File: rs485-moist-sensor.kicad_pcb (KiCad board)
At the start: 2 copper layers, 20 x 140 mm, 26 parts, among them IC1 ATTINY441-MU, P1 CONN_02X03, P2 CONN_01X04, U1 SP3481EN, X1 16MHz

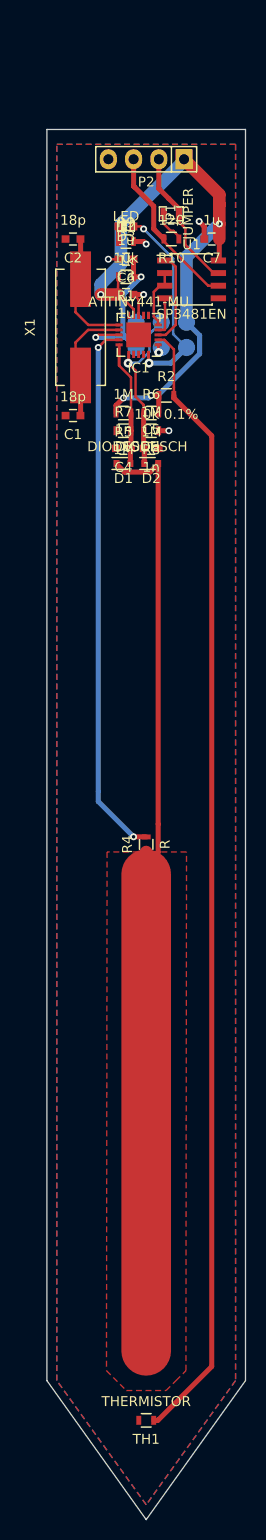
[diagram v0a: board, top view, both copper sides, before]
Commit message: Move trace so that it does not touch a square MOSI pad
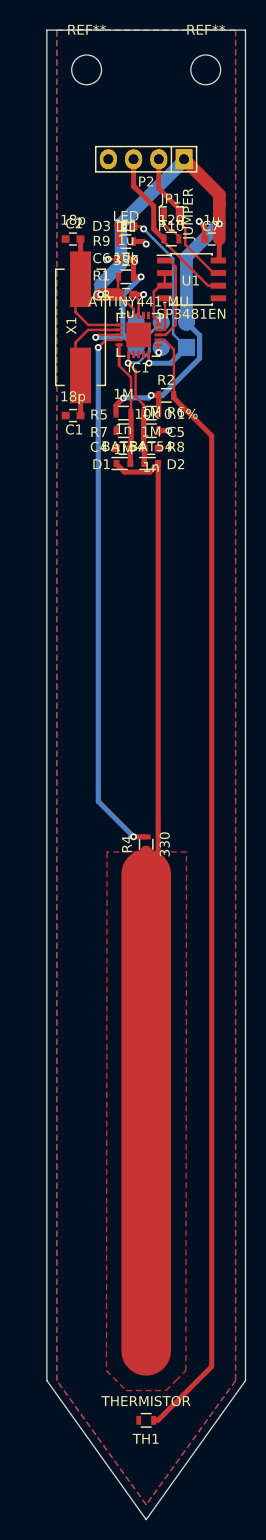
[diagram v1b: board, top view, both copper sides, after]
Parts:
- added REF**: MountingHole_3mm, Mounting_Holes:MountingHole_3mm, F.Cu at (89.0, 17.0)
- added REF**: MountingHole_3mm, Mounting_Holes:MountingHole_3mm, F.Cu at (101.0, 17.0)
- D1, D2: value DIODESCH -> BAT54
- R4: value R -> 330
- R9: value 1k -> 330
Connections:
- U1 pad 1: Net-(IC1-Pad3) -> Net-(IC1-Pad4)
- U1 pad 2: Net-(IC1-Pad5) -> Net-(IC1-Pad3)
- U1 pad 4: Net-(IC1-Pad4) -> Net-(IC1-Pad5)
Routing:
- net Net-(IC1-Pad4): track 3.84 -> 4.66 mm
- net Net-(IC1-Pad5): track 6.14 -> 5.42 mm
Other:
- board size 20 x 140 mm -> 20 x 150 mm

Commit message: Fiddle around with RS485 transceiver lib symbol -- pins were dangerously swapped!
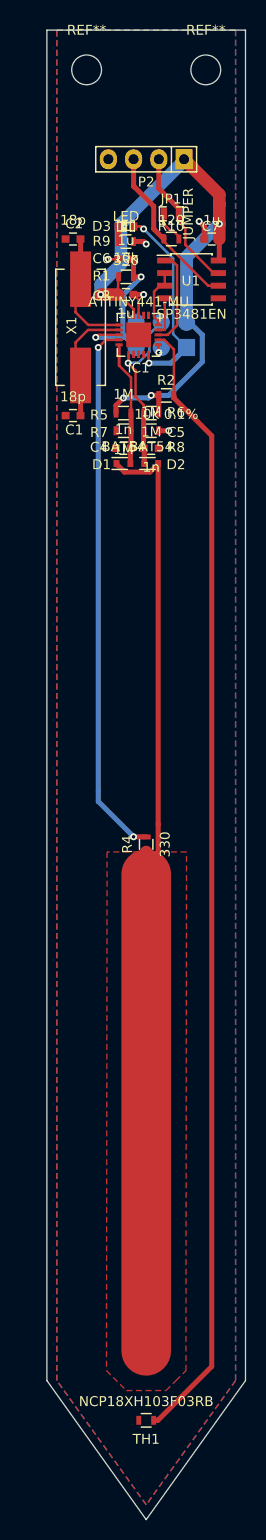
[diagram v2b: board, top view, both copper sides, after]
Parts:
- TH1: value THERMISTOR -> NCP18XH103F03RB
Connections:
- U1 pad 1: Net-(IC1-Pad4) -> Net-(IC1-Pad3)
- U1 pad 2: Net-(IC1-Pad3) -> Net-(IC1-Pad5)
- U1 pad 4: Net-(IC1-Pad5) -> Net-(IC1-Pad4)
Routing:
- net Net-(IC1-Pad5): track 5.42 -> 6.59 mm
- net VCC: track 64.3 -> 65.1 mm

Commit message: Add a local voltage regulator, add antistatic protection, specify transceiver, change attiny441 package to soic-14, route everything
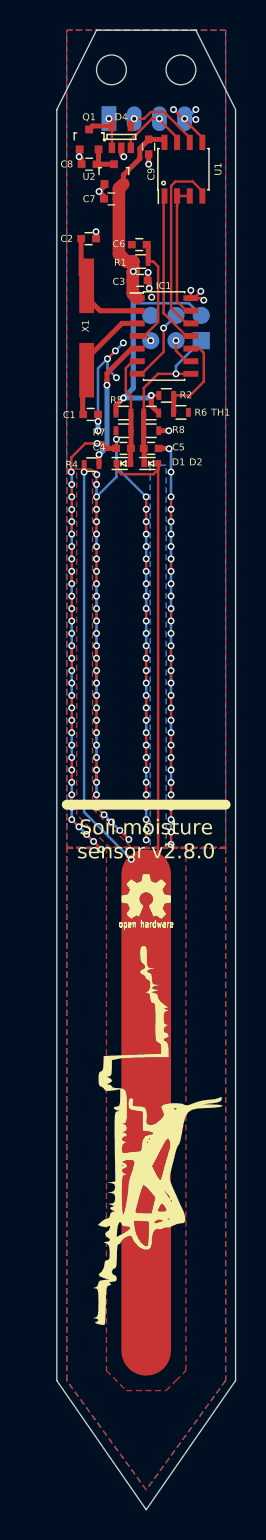
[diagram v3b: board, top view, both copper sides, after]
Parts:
- removed D3: LED, LEDs:LED-0603
- removed JP1: JUMPER, SMD_Packages:SMD-0603_r
- removed R10: 120, Resistors_SMD:R_0603
- removed R9: 330, Resistors_SMD:R_0603
- added C8: 1u, Capacitors_SMD:C_0603, F.Cu at (89.2, 26.5)
- added C9: 1u, Capacitors_SMD:C_0603, F.Cu at (95.2, 24.8)
- added D4: NUP4004M5T1G, Housings_SOT-23_SOT-143_TSOT-6:SOT-23-5, F.Cu at (92.5, 23.8)
- added G***: LOGO, w_logo:Logo_silk_OSHW_6x6mm, F.Cu at (95.0, 100.2)
- added G***: LOGO, chirp_logo:ziogas, B.Cu at (96.2, 124.2)
- added Q1: Q_PMOS_GSD, Housings_SOT-23_SOT-143_TSOT-6:SOT-23, F.Cu at (89.2, 24.0)
- added U2: MCP1702, Housings_SOT-23_SOT-143_TSOT-6:SOT-23, F.Cu at (91.8, 27.5)
- IC1: value ATTINY441-MU -> ATTINY441-SSU; footprint Housings_DFN_QFN:QFN-20-1EP_4x4mm_Pitch0.5mm -> Housings_SOIC:SOIC-14_3.9x8.7mm_Pitch1.27mm
- P1: value CONN_02X03 -> AVR ISP6
- P2: footprint Pin_Headers:Pin_Header_Straight_1x04 -> Pin_Headers:Pin_Header_Straight_1x04_Pitch2.54mm; moved to B.Cu
- U1: value SP3481EN -> SN65HVD72
- moved TH1 101.6 mm to (98.5, 51.5), turned to 0 degrees
- moved R4 38.6 mm to (89.5, 56.8), turned to 0 degrees
- moved U1 11.1 mm to (98.8, 27.0), turned to 90 degrees
- moved C7 10.9 mm to (91.5, 30.0)
- moved P2 5.54 mm to (91.2, 21.9), turned to 270 degrees
- moved IC1 2.57 mm to (96.8, 43.8), turned to 0 degrees
- moved REF** 2.50 mm to (91.5, 17.0)
- moved REF** 2.50 mm to (98.5, 17.0)
- moved R1 2.14 mm to (94.5, 36.3)
- moved C3 2.02 mm to (94.4, 38.2)
- moved C6 1.98 mm to (94.3, 34.6)
- moved C1 1.77 mm to (89.4, 51.7), turned to 0 degrees
- moved P1 1.63 mm to (98.0, 43.0)
- moved C2 1.57 mm to (89.2, 34.0), turned to 0 degrees
- moved X1 0.61 mm to (89.0, 43.0)
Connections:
- C3 pad 1: VCC -> +3V3
- C5 pad 1: /SENSE_HIGH/MOSI -> /SENSE_HIGH/MISO
- C7 pad 1: VCC -> +3V3
- D2 pad 2: /SENSE_HIGH/MOSI -> /SENSE_HIGH/MISO
- IC1 pad 1: /SCK -> +3V3
- IC1 pad 10: (no net) -> /THERMISTOR
- IC1 pad 11: Net-(C2-Pad1) -> Net-(IC1-Pad11)
- IC1 pad 12: Net-(C1-Pad1) -> Net-(IC1-Pad12)
- IC1 pad 13: /RESET -> Net-(IC1-Pad13)
- IC1 pad 14: /EXCITATION -> GND
- IC1 pad 2: /THERMISTOR -> Net-(C2-Pad1)
- IC1 pad 3: Net-(IC1-Pad3) -> Net-(C1-Pad1)
- IC1 pad 4: Net-(IC1-Pad4) -> /RESET
- IC1 pad 5: Net-(IC1-Pad5) -> /EXCITATION
- IC1 pad 6: (no net) -> /SENSE_LOW
- IC1 pad 7: (no net) -> /MOSI
- IC1 pad 8: GND -> /SENSE_HIGH/MISO
- IC1 pad 9: VCC -> /SCK
- P1 pad 1: /MISO -> /SENSE_HIGH/MISO
- P1 pad 2: VCC -> +3V3
- P1 pad 4: /SENSE_HIGH/MOSI -> /MOSI
- P2 pad 2: /RS485B -> /RS485A
- P2 pad 3: /RS485A -> /RS485B
- R1 pad 2: VCC -> +3V3
- R2 pad 1: VCC -> +3V3
- R5 pad 2: VCC -> +3V3
- R6 pad 1: /SENSE_HIGH/MOSI -> /SENSE_HIGH/MISO
- R6 pad 2: VCC -> +3V3
- R8 pad 2: /SENSE_HIGH/MOSI -> /SENSE_HIGH/MISO
- U1 pad 1: Net-(IC1-Pad3) -> Net-(IC1-Pad11)
- U1 pad 2: Net-(IC1-Pad5) -> Net-(IC1-Pad13)
- U1 pad 3: Net-(IC1-Pad5) -> Net-(IC1-Pad13)
- U1 pad 4: Net-(IC1-Pad4) -> Net-(IC1-Pad12)
- U1 pad 8: VCC -> +3V3
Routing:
- net GND: track 8.72 -> 219.9 mm, vias 5 -> 148
- net /THERMISTOR: track 114.1 -> 9.70 mm
- net VCC: track 65.1 -> 5.75 mm, vias 4 -> 1
- net +3V3: track 0.00 -> 48.5 mm, vias 0 -> 3
- net /SENSOR_TRACK: track 98.0 -> 140.8 mm, vias 0 -> 2
- net /EXCITATION: track 54.4 -> 13.6 mm
- net /MISO: track 20.2 -> 0.00 mm, vias 2 -> 0
- net Net-(IC1-Pad12): track 0.00 -> 19.1 mm
- net /SENSE_HIGH/MISO: track 0.00 -> 17.7 mm, vias 0 -> 1
- net /SENSE_HIGH/MOSI: track 17.7 -> 0.00 mm, vias 1 -> 0
- net Net-(IC1-Pad11): track 0.00 -> 15.5 mm
- net Net-(IC1-Pad13): track 0.00 -> 13.7 mm
- net Net-(IC1-Pad3): track 9.79 -> 0.00 mm
- net /RS485A: track 17.2 -> 8.28 mm, vias 0 -> 1
- net /MOSI: track 0.00 -> 7.76 mm, vias 0 -> 1
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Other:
- board size 20 x 150 mm -> 18 x 149 mm
- net class excitation added: clearance 0.6, trace_width 0.254, via_dia 0.7, via_drill 0.4
- board text added: "Catnip Electronics mic@wemakethings.net https://github.com/Miceuz/rs485-moist-sensor"
- board text added: "GND"
- board text added: "RS485-A"
- board text added: "RS485-B"
- board text added: "Soil moisture sensor v2.8.0"
- board text added: "VCC"

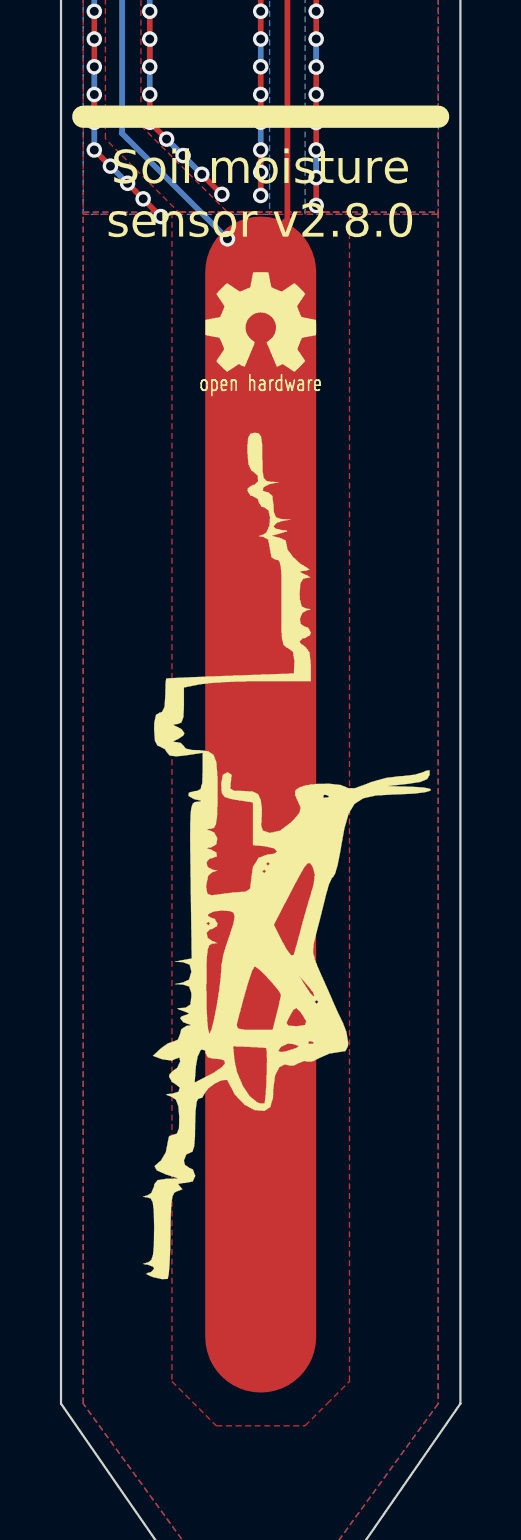
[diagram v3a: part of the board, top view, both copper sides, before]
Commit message: Another board spin - add 3.3v regulator, other rs485 transceiver, esd protection
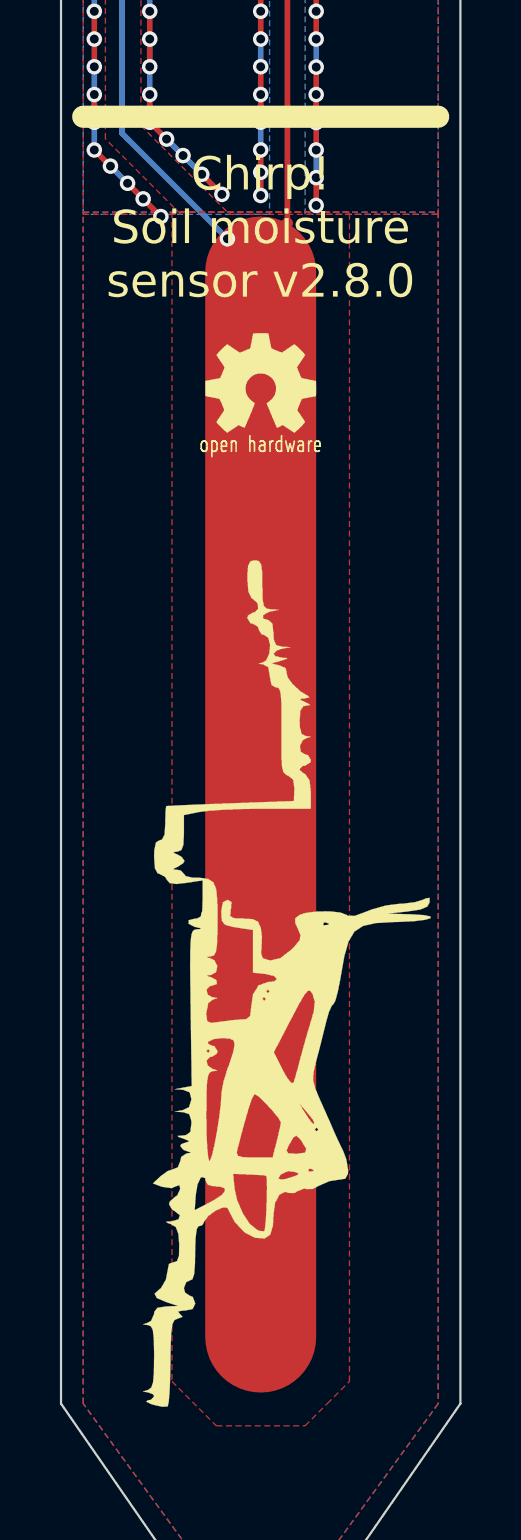
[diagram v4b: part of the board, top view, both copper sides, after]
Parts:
- moved G*** 5.75 mm to (96.2, 130.0)
- moved G*** 2.75 mm to (95.0, 103.0)
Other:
- board text added: "Chirp! Soil moisture sensor v2.8.0"
- board text removed: "Soil moisture sensor v2.8.0"
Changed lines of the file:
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@@
-(kicad_pcb (version 20170123) (host pcbnew no-vcs-found-7589~57~ubuntu14.04.1)
+(kicad_pcb (version 20170123) (host pcbnew no-vcs-found-24a9003~58~ubuntu16.04.1)
   (general
     (links 64)
-    (no_connects 3)
-    (area 85.949999 12.949999 104.050001 162.050001)
+    (no_connects 1)
+    (area 83.111667 11.868 114.755 163.400001)
     (thickness 1.6)
     (drawings 17)
@@
     (47 F.CrtYd user)
     (48 B.Fab user hide)
-    (49 F.Fab user)
+    (49 F.Fab user hide)
   )
   (setup
-    (last_trace_width 0.508)
+    (last_trace_width 0.254)
     (user_trace_width 0.254)
     (user_trace_width 0.508)
@@
     (pad_to_paste_clearance -0.003)
     (aux_axis_origin 0 0)
+    (grid_origin 86 13)
     (visible_elements FFFFFFFF)
     (pcbplotparams
-      (layerselection 0x010f8_80000001)
+      (layerselection 0x010f8_ffffffff)
       (usegerberextensions false)
       (excludeedgelayer true)
@@
   )
   (module w_logo:Logo_silk_OSHW_6x6mm (layer F.Cu)
-    (at 95 100.25)
+    (at 95 103)
     (descr "Open Hardware Logo, 6x6mm")
     (fp_text reference G*** (at 0 0) (layer F.SilkS) hide
@@
   )
   (module chirp_logo:ziogas (layer B.Cu)
-    (at 96.25 124.25 270)
+    (at 96.25 130 270)
     (fp_text reference G*** (at 0 0 270) (layer B.SilkS) hide
       (effects (font (size 0.7 0.7) (thickness 0.11)) (justify mirror))
@@
     (effects (font (size 0.9 0.9) (thickness 0.2)) (justify right mirror))
   )
-  (gr_text "Soil moisture \nsensor v2.8.0" (at 95 94.5) (layer F.SilkS)
+  (gr_text "Chirp!\nSoil moisture \nsensor v2.8.0" (at 95 96) (layer F.SilkS)
     (effects (font (size 1.5 1.5) (thickness 0.3)))
   )
@@
   (segment (start 95.730999 57.719001) (end 92.483001 57.719001) (width 0.254) (layer F.Cu) (net 6))
   (segment (start 92.01 57.246) (end 92.01 56.642) (width 0.254) (layer F.Cu) (net 6))
-  (segment (start 96.204 95.796) (end 94.128468 97.871532) (width 0.508) (layer F.Cu) (net 6))
+  (segment (start 96.204 95.796) (end 94.128468 97.871532) (width 0.508) (layer F.Cu) (net 6) (status 1000000))
+  (segment (start 96.204 92.959962) (end 96.204 95.796) (width 0.254) (layer F.Cu) (net 6) (status 1000000))
+  (segment (start 96.204 56.642) (end 96.204 92.959962) (width 0.254) (layer F.Cu) (net 6) (status 1000000))
   (segment (start 94.128468 97.871532) (end 94 98) (width 0.508) (layer F.Cu) (net 6))
   (segment (start 95 98) (end 94.256936 98) (width 0.508) (layer F.Cu) (net 6))
@@
   (via (at 88.75 57.5) (size 0.7) (drill 0.4) (layers F.Cu B.Cu) (net 6))
   (segment (start 95 98) (end 95 146) (width 5) (layer F.Cu) (net 6))
-  (segment (start 96.204 56.642) (end 96.204 92.959962) (width 0.254) (layer F.Cu) (net 6))
-  (segment (start 96.204 92.959962) (end 96.204 95.796) (width 0.254) (layer F.Cu) (net 6))
   (segment (start 97.778 49.784) (end 97.778 51.472) (width 0.508) (layer F.Cu) (net 7))
   (segment (start 97.778 51.472) (end 97.75 51.5) (width 0.508) (layer F.Cu) (net 7))

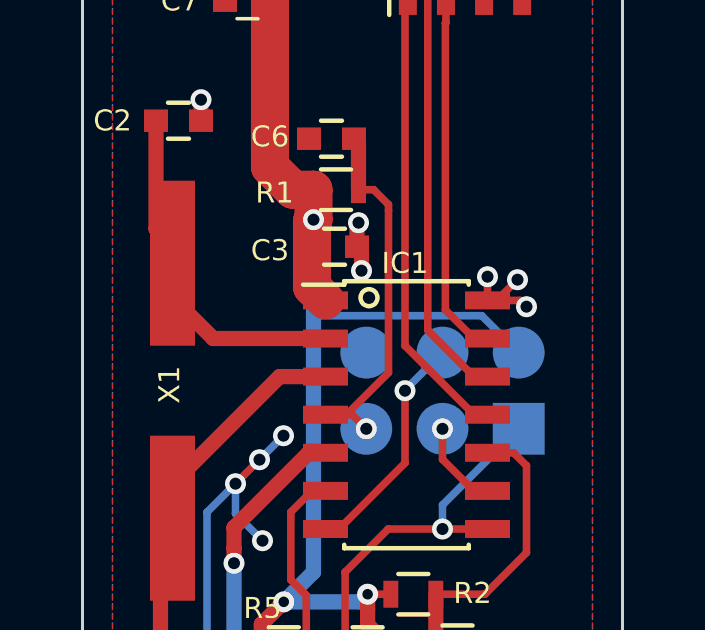
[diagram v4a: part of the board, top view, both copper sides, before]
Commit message: Add a via so that programming header ground is connected
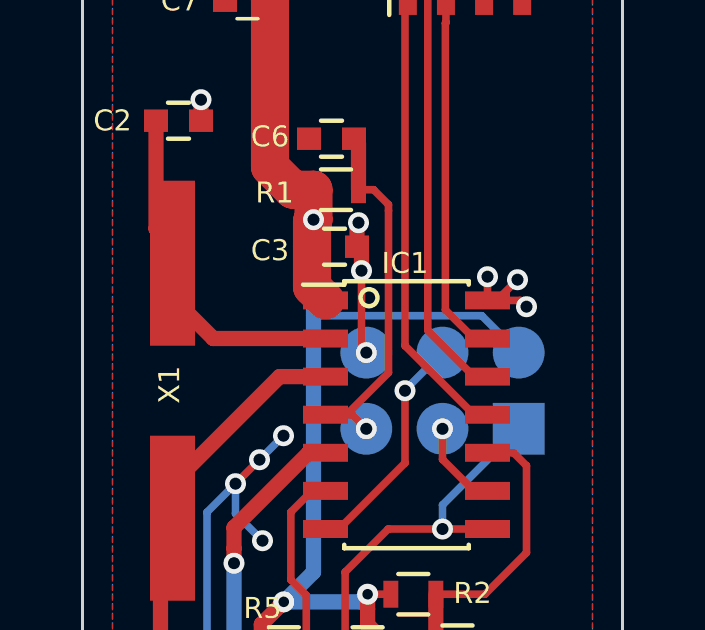
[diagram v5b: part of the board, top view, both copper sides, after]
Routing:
- net GND: track 219.9 -> 222.7 mm, vias 148 -> 149
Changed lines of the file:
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@@
-(kicad_pcb (version 20170123) (host pcbnew no-vcs-found-24a9003~58~ubuntu16.04.1)
+(kicad_pcb (version 20170123) (host pcbnew no-vcs-found-4b5482e~58~ubuntu16.04.1)
   (general
     (links 64)
@@
     (thickness 1.6)
     (drawings 17)
-    (tracks 503)
+    (tracks 506)
     (zones 0)
     (modules 31)
@@
   (segment (start 88.6 51.65) (end 88.6 48.24886) (width 0.508) (layer F.Cu) (net 1))
   (segment (start 88.6 48.24886) (end 89 47.84886) (width 0.508) (layer F.Cu) (net 1))
+  (segment (start 95.3 39) (end 95.3 41.57) (width 0.254) (layer F.Cu) (net 2))
+  (segment (start 95.3 41.57) (end 95.46 41.73) (width 0.254) (layer F.Cu) (net 2))
+  (via (at 95.46 41.73) (size 0.7) (drill 0.4) (layers F.Cu B.Cu) (net 2))
   (via (at 95.25 26.5) (size 0.7) (drill 0.4) (layers F.Cu B.Cu) (net 2))
   (segment (start 95.25 25.5) (end 95.25 26.5) (width 0.508) (layer F.Cu) (net 2))
@@
   (segment (start 95.730999 57.719001) (end 92.483001 57.719001) (width 0.254) (layer F.Cu) (net 6))
   (segment (start 92.01 57.246) (end 92.01 56.642) (width 0.254) (layer F.Cu) (net 6))
-  (segment (start 96.204 95.796) (end 94.128468 97.871532) (width 0.508) (layer F.Cu) (net 6) (status 1000000))
-  (segment (start 96.204 92.959962) (end 96.204 95.796) (width 0.254) (layer F.Cu) (net 6) (status 1000000))
-  (segment (start 96.204 56.642) (end 96.204 92.959962) (width 0.254) (layer F.Cu) (net 6) (status 1000000))
+  (segment (start 96.204 95.796) (end 94.128468 97.871532) (width 0.508) (layer F.Cu) (net 6))
+  (segment (start 96.204 92.959962) (end 96.204 95.796) (width 0.254) (layer F.Cu) (net 6))
+  (segment (start 96.204 56.642) (end 96.204 92.959962) (width 0.254) (layer F.Cu) (net 6))
   (segment (start 94.128468 97.871532) (end 94 98) (width 0.508) (layer F.Cu) (net 6))
   (segment (start 95 98) (end 94.256936 98) (width 0.508) (layer F.Cu) (net 6))
@@
     )
     (polygon
-      (pts        (xy 99 148) (xy 99 95.3) (xy 91 95.3) (xy 91 148) (xy 93 150)
+      (pts
+        (xy 99 148) (xy 99 95.3) (xy 91 95.3) (xy 91 148) (xy 93 150)
         (xy 97 150) (xy 98 149)
       )

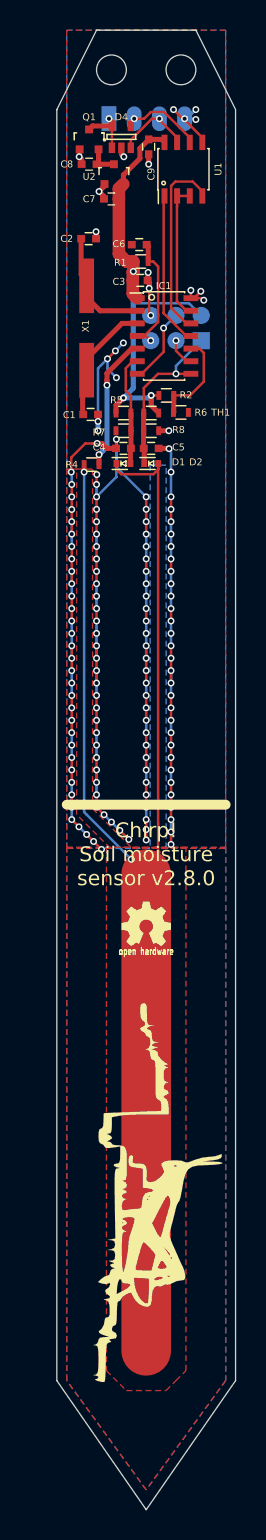
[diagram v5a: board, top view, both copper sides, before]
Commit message: Re-route TVS connection, hook up ground of the programming header
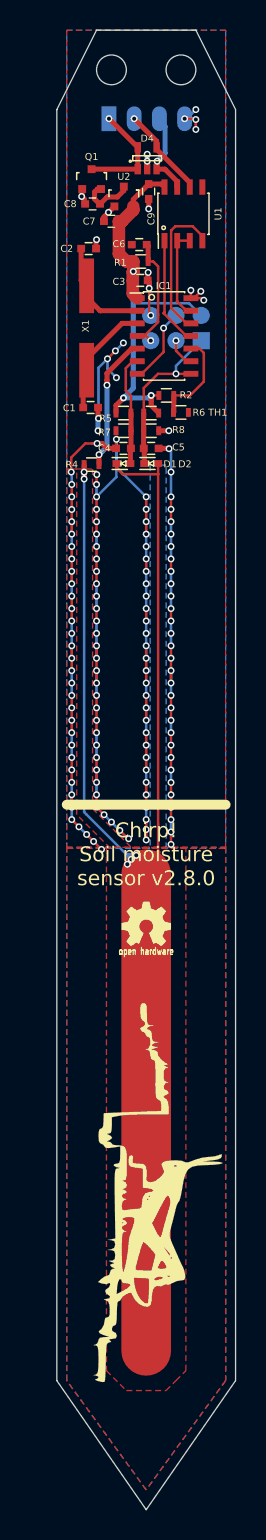
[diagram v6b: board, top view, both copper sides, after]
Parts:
- moved C9 4.50 mm to (95.2, 29.2)
- moved U1 4.50 mm to (98.8, 31.5)
- moved C8 4.02 mm to (89.6, 30.5)
- moved Q1 4.01 mm to (89.5, 28.0)
- moved D4 3.37 mm to (95.1, 25.9)
- moved U2 2.46 mm to (92.8, 29.8)
- moved C7 2.25 mm to (91.5, 32.2)
- moved C2 1.00 mm to (89.2, 35.0)
- moved C1 0.70 mm to (89.4, 51.0)
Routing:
- net VCC: track 5.75 -> 10.9 mm
- net Net-(IC1-Pad13): track 13.7 -> 9.18 mm
- net Net-(IC1-Pad12): track 19.1 -> 14.6 mm
- net /SENSOR_TRACK: track 140.8 -> 145.2 mm, vias 2 -> 5
- net +3V3: track 48.5 -> 44.2 mm
- net Net-(IC1-Pad11): track 15.5 -> 11.7 mm
- net Net-(C8-Pad1): track 3.33 -> 5.59 mm
- net /RS485B: track 8.28 -> 9.88 mm
- net /RS485A: track 8.28 -> 9.67 mm
- net GND: track 222.7 -> 222.1 mm, vias 149 -> 150
